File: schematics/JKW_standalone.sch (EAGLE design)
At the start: 234 parts, among them IC1 4093D, IC4 ATMEGA2560-16AU, Q1 BSS84, Q10 BSS84, Q11 BSS84, Q2 BSS84, Q3 BSS84, Q4 BSS84, Q5 BSS84, Q6 BSS84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

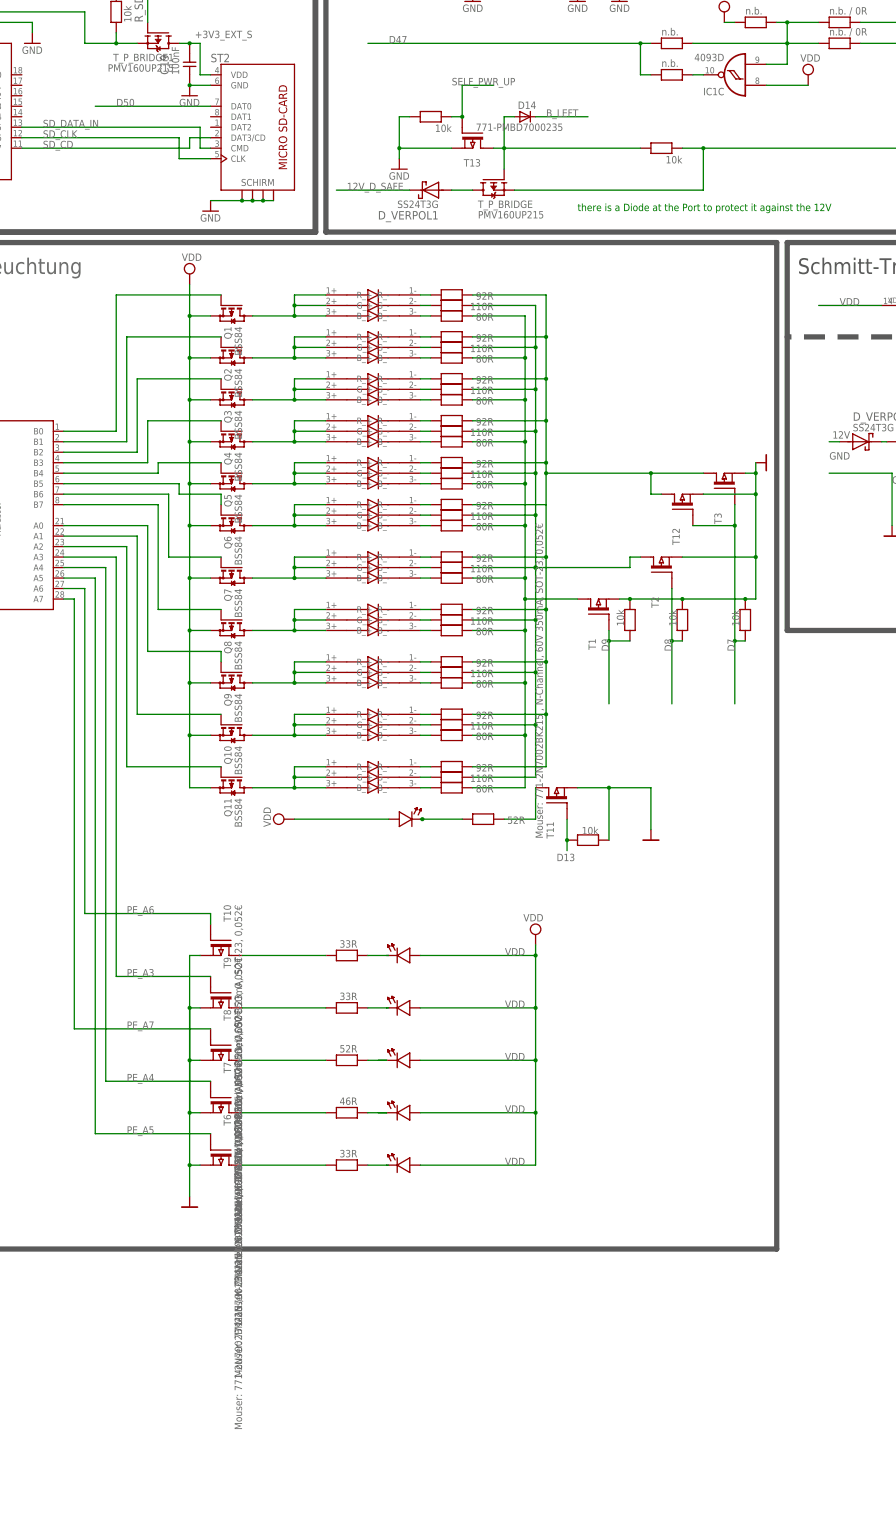
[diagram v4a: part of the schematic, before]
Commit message: cleared the space next to drilling holes
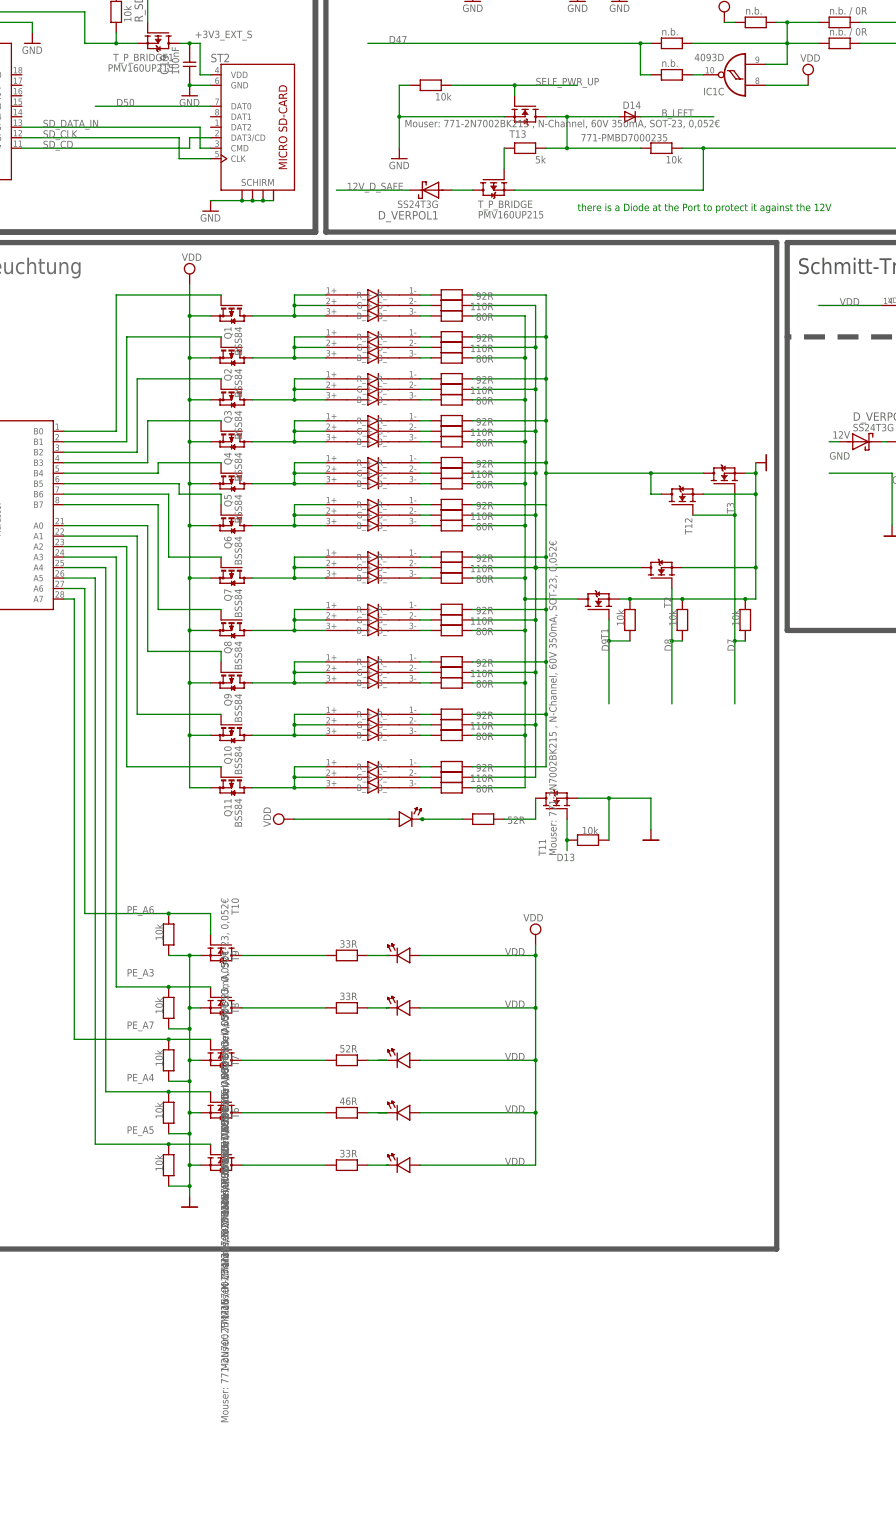
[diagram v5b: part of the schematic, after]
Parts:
- added R_B_LED_16, R_B_LED_17, R_B_LED_18, R_B_LED_19, R_B_LED_20: 10k, RCLDT:R0805
- added R_DEAKT_DAUER_P2: 5k, RCLDT:R0805
- T1, T10, T11, T12, T13, T2, T3, T6, T7, T8, T9: device RCLDT:T-P-FETBSS139 -> Kolja:2N7002
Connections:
- new net N$24: R_DEAKT_DAUER_P2.2, T_P_BRIDGE.G
- net GND: now also R_B_LED_16.1, R_B_LED_17.1, R_B_LED_18.1, R_B_LED_19.1, R_B_LED_20.1
- net NET12: now also R_DEAKT_DAUER_P2.1; no longer T_P_BRIDGE.G
- net PE_A3: now also R_B_LED_17.2
- net PE_A4: now also R_B_LED_19.2
- net PE_A5: now also R_B_LED_20.2
- net PE_A6: now also R_B_LED_16.2
- net PE_A7: now also R_B_LED_18.2
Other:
- moved on the sheet: D14

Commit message: added ground resiistor
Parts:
- added R_BL_L1: n.b., RCLDT:R0805
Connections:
- net A13: now also R_BL_L1.1
- net GND: now also R_BL_L1.2
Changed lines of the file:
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@@
 <?xml version="1.0" encoding="utf-8"?>
 <!DOCTYPE eagle SYSTEM "eagle.dtd">
-<eagle version="6.2">
+<eagle version="6.1">
 <drawing>
 <settings>
@@
 <part name="R_B_LED_20" library="RCLDT" deviceset="R" device="0805" value="10k"/>
 <part name="R_DEAKT_DAUER_P2" library="RCLDT" deviceset="R" device="0805" value="5k "/>
+<part name="R_BL_L1" library="RCLDT" deviceset="R" device="0805" value="n.b."/>
+<part name="GND39" library="SparkFun" deviceset="GND" device=""/>
 </parts>
 <sheets>
@@
 <attribute name="VALUE" x="68.58" y="84.455" size="1.778" layer="96" rot="R180"/>
 </instance>
+<instance part="R_BL_L1" gate="G$1" x="-299.72" y="157.48" smashed="yes" rot="MR0">
+<attribute name="VALUE" x="-297.18" y="159.385" size="1.778" layer="96" rot="MR0"/>
+</instance>
+<instance part="GND39" gate="1" x="-307.34" y="152.4"/>
 </instances>
 <busses>
@@
 <junction x="33.02" y="93.98"/>
 </segment>
+<segment>
+<pinref part="R_BL_L1" gate="G$1" pin="2"/>
+<pinref part="GND39" gate="1" pin="GND"/>
+<wire x1="-304.8" y1="157.48" x2="-307.34" y2="157.48" width="0.1524" layer="91"/>
+<wire x1="-307.34" y1="157.48" x2="-307.34" y2="154.94" width="0.1524" layer="91"/>
+</segment>
 </net>
 <net name="DZ" class="0">
@@
 <pinref part="IC4" gate="1" pin="PK5(ADC13/PCINT21)"/>
 <pinref part="TX1" gate="G$1" pin="1"/>
-<wire x1="-256.54" y1="147.32" x2="-289.56" y2="147.32" width="0.1524" layer="91"/>
+<wire x1="-256.54" y1="147.32" x2="-281.94" y2="147.32" width="0.1524" layer="91"/>
 <pinref part="TX2" gate="G$1" pin="1"/>
+<wire x1="-281.94" y1="147.32" x2="-289.56" y2="147.32" width="0.1524" layer="91"/>
 <wire x1="-289.56" y1="147.32" x2="-299.72" y2="147.32" width="0.1524" layer="91"/>
 <junction x="-289.56" y="147.32"/>
-</segment>
-</net>
+<pinref part="R_BL_L1" gate="G$1" pin="1"/>
+<wire x1="-294.64" y1="157.48" x2="-281.94" y2="157.48" width="0.1524" layer="91"/>
+<wire x1="-281.94" y1="157.48" x2="-281.94" y2="147.32" width="0.1524" layer="91"/>
+<junction x="-281.94" y="147.32"/>
+</segment>
+</net>

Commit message: rearrangedparts
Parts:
- CP1, CP2, CP3, CP4: value 220µF/16V -> 330µF/16V
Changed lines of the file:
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@@
 <?xml version="1.0" encoding="utf-8"?>
 <!DOCTYPE eagle SYSTEM "eagle.dtd">
-<eagle version="6.1">
+<eagle version="6.2">
 <drawing>
 <settings>
@@
 <part name="GND25" library="supply1" deviceset="GND" device=""/>
 <part name="GND26" library="supply1" deviceset="GND" device=""/>
-<part name="CP1" library="Kolja" deviceset="C_SMD_SMP" device="" value="220µF/16V"/>
-<part name="CP2" library="Kolja" deviceset="C_SMD_SMP" device="" value="220µF/16V"/>
+<part name="CP1" library="Kolja" deviceset="C_SMD_SMP" device="" value="330µF/16V"/>
+<part name="CP2" library="Kolja" deviceset="C_SMD_SMP" device="" value="330µF/16V"/>
 <part name="U$15" library="SUPPLY" deviceset="GND" device=""/>
-<part name="CP3" library="Kolja" deviceset="C_SMD_SMP" device="" value="220µF/16V"/>
-<part name="CP4" library="Kolja" deviceset="C_SMD_SMP" device="" value="220µF/16V"/>
+<part name="CP3" library="Kolja" deviceset="C_SMD_SMP" device="" value="330µF/16V"/>
+<part name="CP4" library="Kolja" deviceset="C_SMD_SMP" device="" value="330µF/16V"/>
 <part name="D3" library="diode" deviceset="ZENER-DIODE" device="SOT23" value="5.5V"/>
 <part name="GND27" library="supply1" deviceset="GND" device=""/>

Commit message: Final design 7
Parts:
- PWR, TX2: device pinhead:PINHD-1X2 -> pinhead:PINHD-1X3
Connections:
- net +3V3_EXT: now also PWR.1
- net A12: no longer TX2.2
- net GND: now also PWR.3; no longer PWR.1
- net SCL: now also TX2.3
- net SDA: now also TX2.2
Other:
- moved on the sheet: JP1, TX1
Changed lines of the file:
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@@
 <?xml version="1.0" encoding="utf-8"?>
 <!DOCTYPE eagle SYSTEM "eagle.dtd">
-<eagle version="6.2">
+<eagle version="6.1">
 <drawing>
 <settings>
@@
 <part name="U$18" library="SUPPLY" deviceset="GND" device=""/>
 <part name="C4" library="RCLDT" deviceset="C" device="0805" value="100nF"/>
-<part name="PWR" library="pinhead" deviceset="PINHD-1X2" device=""/>
+<part name="PWR" library="pinhead" deviceset="PINHD-1X3" device=""/>
 <part name="PWR1" library="pinhead" deviceset="PINHD-1X2" device=""/>
 <part name="R_HB1" library="RCLDT" deviceset="R" device="0805" value="600R"/>
@@
 <part name="D12" library="semicon-smd-ipc" deviceset="D-" device="A1-C3" value="771-PMBD7000235"/>
 <part name="T_P_BRIDGE" library="Kolja" deviceset="PMV160UP215" device=""/>
-<part name="TX2" library="pinhead" deviceset="PINHD-1X2" device=""/>
+<part name="TX2" library="pinhead" deviceset="PINHD-1X3" device=""/>
 <part name="T_P_BRIDGE1" library="Kolja" deviceset="PMV160UP215" device=""/>
 <part name="D14" library="semicon-smd-ipc" deviceset="D-" device="A1-C3" value="771-PMBD7000235"/>
@@
 <text x="-322.58" y="243.84" size="5.08" layer="95">ATmega2560</text>
 <text x="-175.26" y="160.02" size="1.6764" layer="91">D18</text>
-<text x="-317.5" y="106.68" size="1.778" layer="91" rot="R90">MISO</text>
-<text x="-314.96" y="132.08" size="1.778" layer="91" rot="R90">MOSI</text>
-<text x="-314.96" y="106.68" size="1.778" layer="91" rot="R90">SCK</text>
-<text x="-312.42" y="132.08" size="1.778" layer="91" rot="R90">GND</text>
-<text x="-317.5" y="132.08" size="1.778" layer="91" rot="R90">VDD</text>
-<text x="-312.42" y="106.68" size="1.778" layer="91" rot="R90">RST</text>
+<text x="-320.04" y="91.44" size="1.778" layer="91" rot="R90">MISO</text>
+<text x="-317.5" y="116.84" size="1.778" layer="91" rot="R90">MOSI</text>
+<text x="-317.5" y="91.44" size="1.778" layer="91" rot="R90">SCK</text>
+<text x="-314.96" y="116.84" size="1.778" layer="91" rot="R90">GND</text>
+<text x="-320.04" y="116.84" size="1.778" layer="91" rot="R90">VDD</text>
+<text x="-314.96" y="91.44" size="1.778" layer="91" rot="R90">RST</text>
 <text x="-144.78" y="-17.78" size="1.778" layer="91">ATm2560 alive toggle</text>
 <text x="10.668" y="170.688" size="1.778" layer="91" rot="R90">ARD_RX</text>
@@
 <instance part="16MHZ" gate="G$1" x="-261.62" y="231.14" rot="R90"/>
 <instance part="GND7" gate="1" x="-281.94" y="228.6" rot="R270"/>
-<instance part="JP1" gate="A" x="-314.96" y="124.46" rot="R270"/>
+<instance part="JP1" gate="A" x="-317.5" y="109.22" rot="R270"/>
 <instance part="SUPPLY4" gate="G$1" x="-279.4" y="205.74" rot="R90"/>
 <instance part="SUPPLY5" gate="G$1" x="-294.64" y="218.44"/>
@@
 <instance part="SUPPLY3" gate="G$1" x="358.14" y="238.76"/>
 <instance part="SUPPLY9" gate="G$1" x="60.96" y="246.38"/>
-<instance part="TX1" gate="G$1" x="-297.18" y="144.78"/>
+<instance part="TX1" gate="G$1" x="-289.56" y="144.78"/>
 <instance part="R_DZ_DOWN" gate="G$1" x="81.28" y="236.22" rot="MR90"/>
 <instance part="C8" gate="C" x="71.12" y="236.22" smashed="yes" rot="MR90">
@@
 <instance part="U$18" gate="G$1" x="-119.38" y="-2.54"/>
 <instance part="C4" gate="C" x="-93.98" y="218.44" rot="R180"/>
-<instance part="PWR" gate="G$1" x="259.08" y="55.88" rot="R180"/>
+<instance part="PWR" gate="A" x="254" y="53.34" rot="R180"/>
 <instance part="PWR1" gate="G$1" x="281.94" y="55.88" rot="R180"/>
 <instance part="R_HB1" gate="G$1" x="91.44" y="203.2" rot="R180"/>
@@
 <attribute name="NAME" x="52.07" y="73.66" size="1.778" layer="95" rot="MR180"/>
 </instance>
-<instance part="TX2" gate="G$1" x="-287.02" y="144.78"/>
+<instance part="TX2" gate="A" x="-307.34" y="144.78"/>
 <instance part="T_P_BRIDGE1" gate="G$1" x="-25.4" y="114.3" smashed="yes" rot="R270">
 <attribute name="VALUE" x="-21.59" y="106.68" size="1.778" layer="96" rot="R180"/>
@@
 </segment>
 <segment>
-<wire x1="-312.42" y1="127" x2="-312.42" y2="147.32" width="0.1524" layer="91"/>
-<label x="-312.5978" y="139.5222" size="1.778" layer="95" rot="R90"/>
+<wire x1="-314.96" y1="111.76" x2="-314.96" y2="132.08" width="0.1524" layer="91"/>
+<label x="-315.1378" y="124.2822" size="1.778" layer="95" rot="R90"/>
 <pinref part="JP1" gate="A" pin="1"/>
 </segment>
@@
 </segment>
 <segment>
-<pinref part="PWR" gate="G$1" pin="1"/>
-<wire x1="261.62" y1="53.34" x2="274.32" y2="53.34" width="0.1524" layer="91"/>
-<label x="266.7" y="53.34" size="1.778" layer="95"/>
-</segment>
-<segment>
 <pinref part="PWR1" gate="G$1" pin="1"/>
 <wire x1="284.48" y1="53.34" x2="297.18" y2="53.34" width="0.1524" layer="91"/>
@@
 <wire x1="-307.34" y1="157.48" x2="-307.34" y2="154.94" width="0.1524" layer="91"/>
 </segment>
+<segment>
+<pinref part="PWR" gate="A" pin="3"/>
+<wire x1="256.54" y1="55.88" x2="269.24" y2="55.88" width="0.1524" layer="91"/>
+<label x="261.62" y="55.88" size="1.778" layer="95"/>
+</segment>
 </net>
 <net name="DZ" class="0">
@@
 </segment>
 <segment>
-<wire x1="-317.5" y1="127" x2="-317.5" y2="147.32" width="0.1524" layer="91"/>
-<label x="-317.7286" y="139.2174" size="1.778" layer="95" rot="R90"/>
+<wire x1="-320.04" y1="111.76" x2="-320.04" y2="132.08" width="0.1524" layer="91"/>
+<label x="-320.2686" y="123.9774" size="1.778" layer="95" rot="R90"/>
 <pinref part="JP1" gate="A" pin="5"/>
 </segment>
@@
 </segment>
 <segment>
-<pinref part="PWR" gate="G$1" pin="2"/>
-<wire x1="261.62" y1="55.88" x2="274.32" y2="55.88" width="0.1524" layer="91"/>
-<label x="266.7" y="55.88" size="1.778" layer="95"/>
+<pinref part="PWR" gate="A" pin="2"/>
+<wire x1="256.54" y1="53.34" x2="269.24" y2="53.34" width="0.1524" layer="91"/>
+<label x="261.62" y="53.34" size="1.778" layer="95"/>
 </segment>
 <segment>
@@
 <pinref part="T_P_BRIDGE1" gate="G$1" pin="S"/>
 </segment>
+<segment>
+<pinref part="PWR" gate="A" pin="1"/>
+<wire x1="256.54" y1="50.8" x2="269.24" y2="50.8" width="0.1524" layer="91"/>
+<label x="261.62" y="50.8" size="1.778" layer="95"/>
+</segment>
 </net>
 <net name="ARD_RES_OUT" class="0">
 <segment>
-<wire x1="-312.42" y1="119.38" x2="-312.42" y2="93.98" width="0.1524" layer="91"/>
-<label x="-312.7248" y="96.4184" size="1.778" layer="95" rot="R90"/>
+<wire x1="-314.96" y1="104.14" x2="-314.96" y2="78.74" width="0.1524" layer="91"/>
+<label x="-315.2648" y="81.1784" size="1.778" layer="95" rot="R90"/>
 <pinref part="JP1" gate="A" pin="2"/>
 </segment>
@@
 <pinref part="TX1" gate="G$1" pin="1"/>
 <wire x1="-256.54" y1="147.32" x2="-281.94" y2="147.32" width="0.1524" layer="91"/>
-<pinref part="TX2" gate="G$1" pin="1"/>
-<wire x1="-281.94" y1="147.32" x2="-289.56" y2="147.32" width="0.1524" layer="91"/>
-<wire x1="-289.56" y1="147.32" x2="-299.72" y2="147.32" width="0.1524" layer="91"/>
-<junction x="-289.56" y="147.32"/>
+<pinref part="TX2" gate="A" pin="1"/>
+<wire x1="-281.94" y1="147.32" x2="-309.88" y2="147.32" width="0.1524" layer="91"/>
+<wire x1="-309.88" y1="147.32" x2="-292.1" y2="147.32" width="0.1524" layer="91"/>
+<junction x="-309.88" y="147.32"/>
 <pinref part="R_BL_L1" gate="G$1" pin="1"/>
 <wire x1="-294.64" y1="157.48" x2="-281.94" y2="157.48" width="0.1524" layer="91"/>
@@
 <pinref part="IC4" gate="1" pin="PK4(ADC12/PCINT20)"/>
 <pinref part="TX1" gate="G$1" pin="2"/>
-<wire x1="-256.54" y1="144.78" x2="-289.56" y2="144.78" width="0.1524" layer="91"/>
-<pinref part="TX2" gate="G$1" pin="2"/>
-<wire x1="-289.56" y1="144.78" x2="-299.72" y2="144.78" width="0.1524" layer="91"/>
-<junction x="-289.56" y="144.78"/>
+<wire x1="-256.54" y1="144.78" x2="-292.1" y2="144.78" width="0.1524" layer="91"/>
 </segment>
 </net>
@@
 </segment>
 <segment>
-<wire x1="-314.96" y1="119.38" x2="-314.96" y2="93.98" width="0.1524" layer="91"/>
-<label x="-315.1886" y="96.7232" size="1.778" layer="95" rot="R90"/>
+<wire x1="-317.5" y1="104.14" x2="-317.5" y2="78.74" width="0.1524" layer="91"/>
+<label x="-317.7286" y="81.4832" size="1.778" layer="95" rot="R90"/>
 <pinref part="JP1" gate="A" pin="4"/>
 </segment>
@@
 </segment>
 <segment>
-<wire x1="-314.96" y1="127" x2="-314.96" y2="147.32" width="0.1524" layer="91"/>
-<label x="-315.2394" y="139.3952" size="1.778" layer="95" rot="R90"/>
+<wire x1="-317.5" y1="111.76" x2="-317.5" y2="132.08" width="0.1524" layer="91"/>
+<label x="-317.7794" y="124.1552" size="1.778" layer="95" rot="R90"/>
 <pinref part="JP1" gate="A" pin="3"/>
 </segment>
@@
 </segment>
 <segment>
-<wire x1="-317.5" y1="119.38" x2="-317.5" y2="93.98" width="0.1524" layer="91"/>
-<label x="-317.7286" y="96.8756" size="1.778" layer="95" rot="R90"/>
+<wire x1="-320.04" y1="104.14" x2="-320.04" y2="78.74" width="0.1524" layer="91"/>
+<label x="-320.2686" y="81.6356" size="1.778" layer="95" rot="R90"/>
 <pinref part="JP1" gate="A" pin="6"/>
 </segment>
@@
 <label x="-99.06" y="-22.86" size="1.778" layer="95"/>
 </segment>
+<segment>
+<pinref part="TX2" gate="A" pin="2"/>
+<wire x1="-309.88" y1="144.78" x2="-322.58" y2="144.78" width="0.1524" layer="91"/>
+<label x="-322.58" y="144.78" size="1.778" layer="95"/>
+</segment>
 </net>
 <net name="SCL" class="0">
@@
 <label x="-99.06" y="-20.32" size="1.778" layer="95"/>
 </segment>
+<segment>
+<pinref part="TX2" gate="A" pin="3"/>
+<wire x1="-309.88" y1="142.24" x2="-322.58" y2="142.24" width="0.1524" layer="91"/>
+<label x="-322.58" y="142.24" size="1.778" layer="95"/>
+</segment>
 </net>
